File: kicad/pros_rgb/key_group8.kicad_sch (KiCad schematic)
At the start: 16 parts

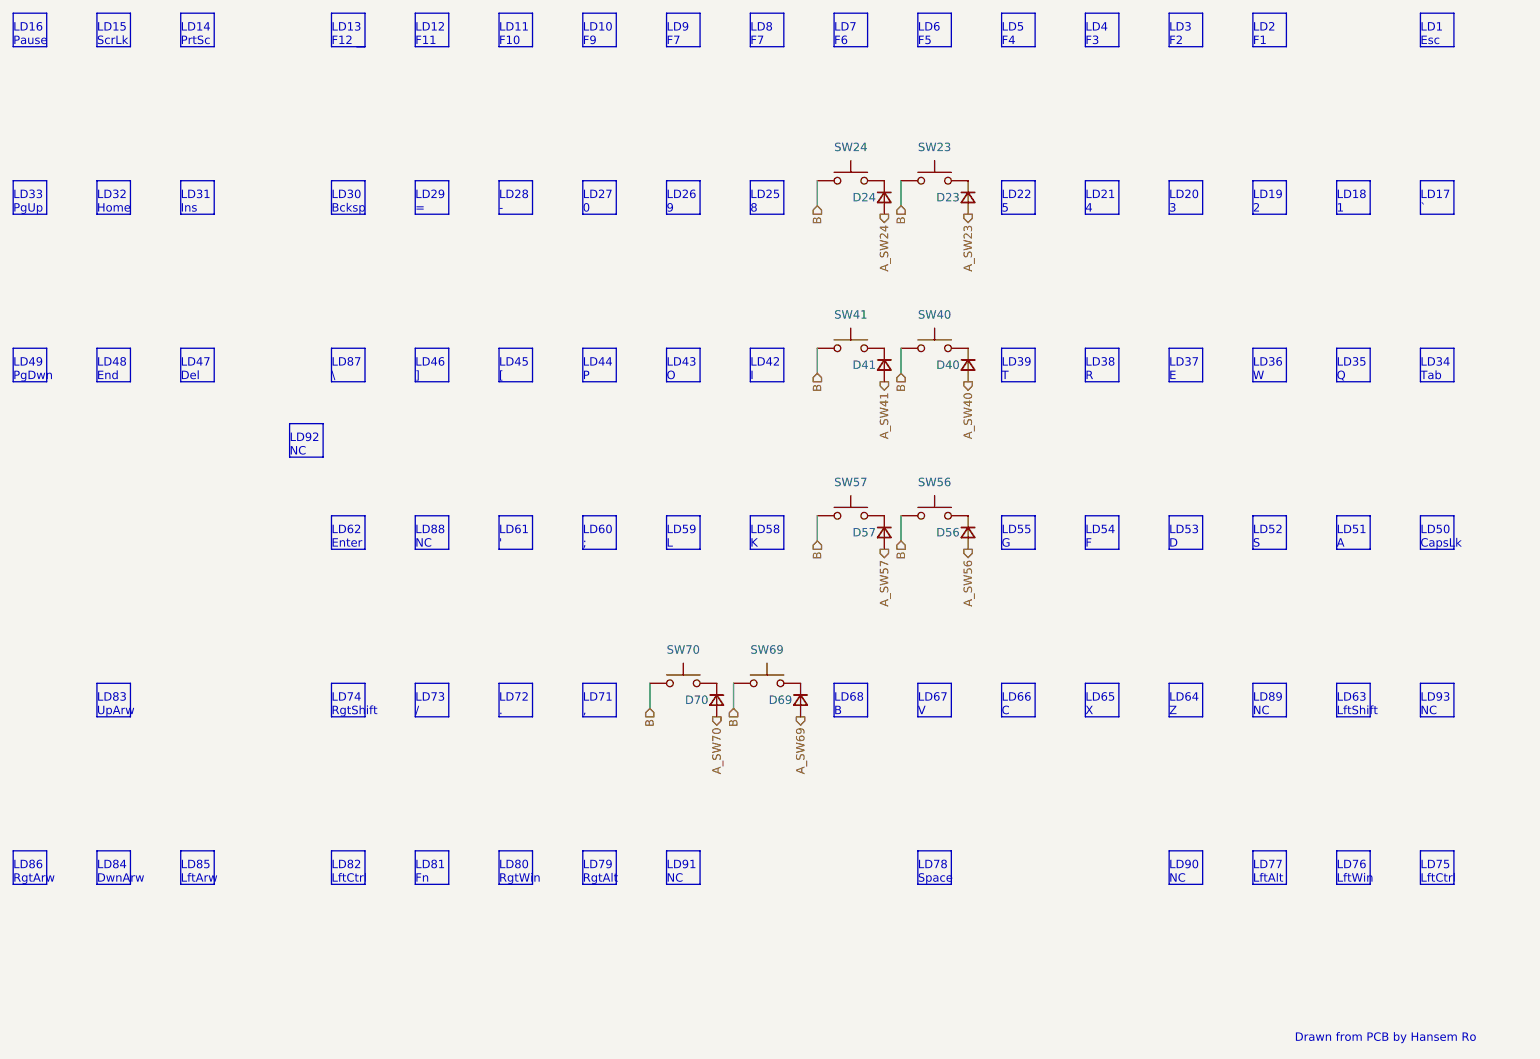
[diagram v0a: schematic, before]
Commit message: kicad/pros_rgb: update key groupings
These new groupings are based off ordering in firmware:
https://github.com/hansemro/pok3r_re_firmware/blob/4b68aa4baf7d28dc8dbf8eebcb1fdb59e7bcd629/disassemble/cmprosrgb/v122/cmprosrgb_v122.txt#L14599-L14629
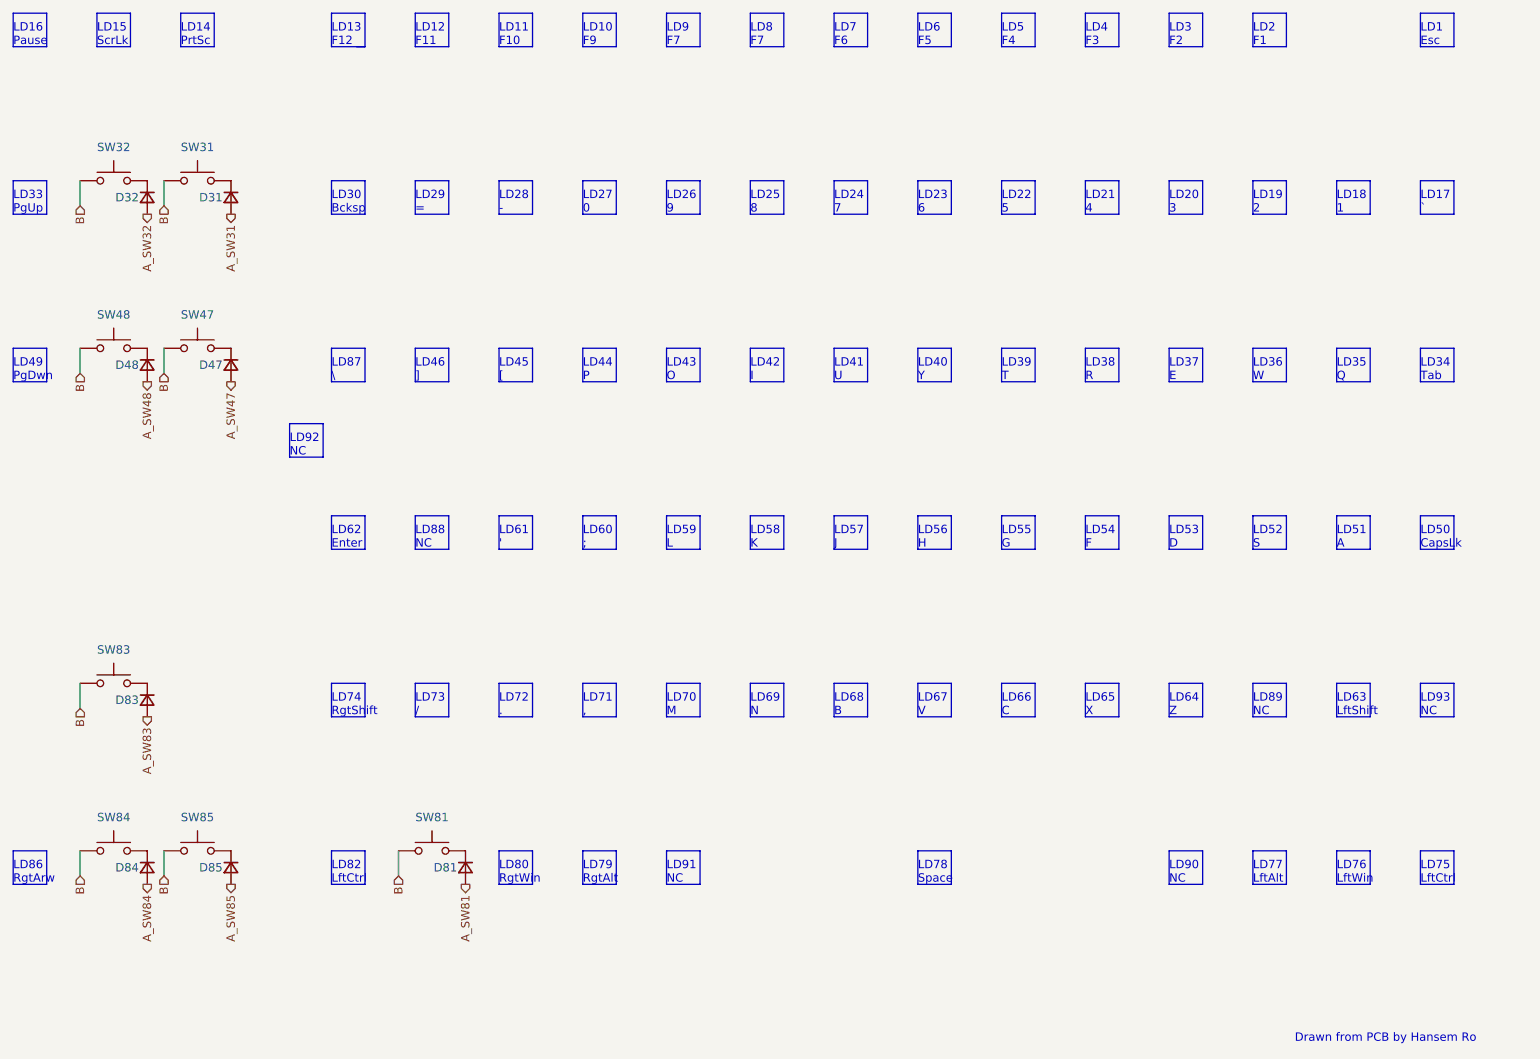
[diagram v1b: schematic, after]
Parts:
- removed D23, D24, D40, D41, D56, D57, D69, D70: ~, symbol Device:D_Small
- removed SW23, SW24, SW40, SW41, SW56, SW57, SW69, SW70: ~, symbol Switch:SW_Push
- added D31, D32, D47, D48, D81, D83, D84, D85: (no value), symbol Device:D_Small
- added SW31, SW32, SW47, SW48, SW81, SW83, SW84, SW85: (no value), symbol Switch:SW_Push
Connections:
- net B: now also SW31.1, SW32.1, SW47.1, SW48.1, SW81.1, SW83.1, SW84.1, SW85.1
- new net: D32.1 (K), SW32.2
- new net: D81.1 (K), SW81.2
- new net: D85.1 (K), SW85.2
- new net: D84.1 (K), SW84.2
- new net: D31.1 (K), SW31.2
- new net: D47.1 (K), SW47.2
- new net: D83.1 (K), SW83.2
- new net: D48.1 (K), SW48.2
- new net A_SW31: D31.2 (A)
- new net A_SW32: D32.2 (A)
- new net A_SW47: D47.2 (A)
- new net A_SW48: D48.2 (A)
- new net A_SW81: D81.2 (A)
- new net A_SW83: D83.2 (A)
- new net A_SW84: D84.2 (A)
- new net A_SW85: D85.2 (A)
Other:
- note added: "LD23 6"
- note added: "LD24 7"
- note added: "LD40 Y"
- note added: "LD41 U"
- note added: "LD56 H"
- note added: "LD57 J"
- note added: "LD69 N"
- note added: "LD70 M"
- note removed: "LD31 Ins"
- note removed: "LD32 Home"
- note removed: "LD47 Del"
- note removed: "LD48 End"
- note removed: "LD81 Fn"
- note removed: "LD83 UpArw"
- note removed: "LD84 DwnArw"
- note removed: "LD85 LftArw"

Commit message: kicad/pros_rgb: mark as Rev. B
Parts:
- D31, D32, D47, D48, D81, D83, D84, D85, SW31, SW32, SW47, SW48, SW81, SW83, SW84, SW85: value (none) -> ~
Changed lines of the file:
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@@
       (effects (font (size 1.27 1.27)) (justify right))
     )
-    (property "Value" "" (id 1) (at 81.28 53.3399 90)
+    (property "Value" "~" (id 1) (at 81.28 53.3399 90)
       (effects (font (size 1.27 1.27)) (justify left))
     )
@@
       (effects (font (size 1.27 1.27)) (justify right))
     )
-    (property "Value" "" (id 1) (at 129.54 154.9399 90)
+    (property "Value" "~" (id 1) (at 129.54 154.9399 90)
       (effects (font (size 1.27 1.27)) (justify left))
     )
@@
     (in_bom yes) (on_board yes)
     (property "Reference" "SW32" (id 0) (at 73.66 44.45 0))
-    (property "Value" "" (id 1) (at 73.66 44.45 0))
+    (property "Value" "~" (id 1) (at 73.66 44.45 0))
     (property "Footprint" "" (id 2) (at 73.66 44.45 0)
       (effects (font (size 1.27 1.27)) hide)
@@
     (in_bom yes) (on_board yes)
     (property "Reference" "SW85" (id 0) (at 86.36 146.05 0))
-    (property "Value" "" (id 1) (at 86.36 146.05 0))
+    (property "Value" "~" (id 1) (at 86.36 146.05 0))
     (property "Footprint" "" (id 2) (at 86.36 146.05 0)
       (effects (font (size 1.27 1.27)) hide)
@@
     (in_bom yes) (on_board yes)
     (property "Reference" "SW84" (id 0) (at 73.66 146.05 0))
-    (property "Value" "" (id 1) (at 73.66 146.05 0))
+    (property "Value" "~" (id 1) (at 73.66 146.05 0))
     (property "Footprint" "" (id 2) (at 73.66 146.05 0)
       (effects (font (size 1.27 1.27)) hide)
@@
       (effects (font (size 1.27 1.27)) (justify right))
     )
-    (property "Value" "" (id 1) (at 93.98 53.3399 90)
+    (property "Value" "~" (id 1) (at 93.98 53.3399 90)
       (effects (font (size 1.27 1.27)) (justify left))
     )
@@
     (in_bom yes) (on_board yes)
     (property "Reference" "SW47" (id 0) (at 86.36 69.85 0))
-    (property "Value" "" (id 1) (at 86.36 69.85 0))
+    (property "Value" "~" (id 1) (at 86.36 69.85 0))
     (property "Footprint" "" (id 2) (at 86.36 69.85 0)
       (effects (font (size 1.27 1.27)) hide)
@@
       (effects (font (size 1.27 1.27)) (justify right))
     )
-    (property "Value" "" (id 1) (at 81.28 129.5399 90)
+    (property "Value" "~" (id 1) (at 81.28 129.5399 90)
       (effects (font (size 1.27 1.27)) (justify left))
     )
@@
     (in_bom yes) (on_board yes)
     (property "Reference" "SW48" (id 0) (at 73.66 69.85 0))
-    (property "Value" "" (id 1) (at 73.66 69.85 0))
+    (property "Value" "~" (id 1) (at 73.66 69.85 0))
     (property "Footprint" "" (id 2) (at 73.66 69.85 0)
       (effects (font (size 1.27 1.27)) hide)
@@
     (in_bom yes) (on_board yes)
     (property "Reference" "SW31" (id 0) (at 86.36 44.45 0))
-    (property "Value" "" (id 1) (at 86.36 44.45 0))
+    (property "Value" "~" (id 1) (at 86.36 44.45 0))
     (property "Footprint" "" (id 2) (at 86.36 44.45 0)
       (effects (font (size 1.27 1.27)) hide)
@@
       (effects (font (size 1.27 1.27)) (justify right))
     )
-    (property "Value" "" (id 1) (at 81.28 154.9399 90)
+    (property "Value" "~" (id 1) (at 81.28 154.9399 90)
       (effects (font (size 1.27 1.27)) (justify left))
     )
@@
     (in_bom yes) (on_board yes)
     (property "Reference" "SW81" (id 0) (at 121.92 146.05 0))
-    (property "Value" "" (id 1) (at 121.92 146.05 0))
+    (property "Value" "~" (id 1) (at 121.92 146.05 0))
     (property "Footprint" "" (id 2) (at 121.92 146.05 0)
       (effects (font (size 1.27 1.27)) hide)
@@
       (effects (font (size 1.27 1.27)) (justify right))
     )
-    (property "Value" "" (id 1) (at 93.98 154.9399 90)
+    (property "Value" "~" (id 1) (at 93.98 154.9399 90)
       (effects (font (size 1.27 1.27)) (justify left))
     )
@@
     (in_bom yes) (on_board yes)
     (property "Reference" "SW83" (id 0) (at 73.66 120.65 0))
-    (property "Value" "" (id 1) (at 73.66 120.65 0))
+    (property "Value" "~" (id 1) (at 73.66 120.65 0))
     (property "Footprint" "" (id 2) (at 73.66 120.65 0)
       (effects (font (size 1.27 1.27)) hide)
@@
       (effects (font (size 1.27 1.27)) (justify right))
     )
-    (property "Value" "" (id 1) (at 81.28 78.7399 90)
+    (property "Value" "~" (id 1) (at 81.28 78.7399 90)
       (effects (font (size 1.27 1.27)) (justify left))
     )
@@
       (effects (font (size 1.27 1.27)) (justify right))
     )
-    (property "Value" "" (id 1) (at 93.98 78.7399 90)
-      (effects (font (size 1.27 1.27)) (justify left))
-    )
+    (property "Value" "~" (id 1) (at 93.98 78.7399 90)
+      (effects (font (size 1.27 1.27)) (justify left))
+    )

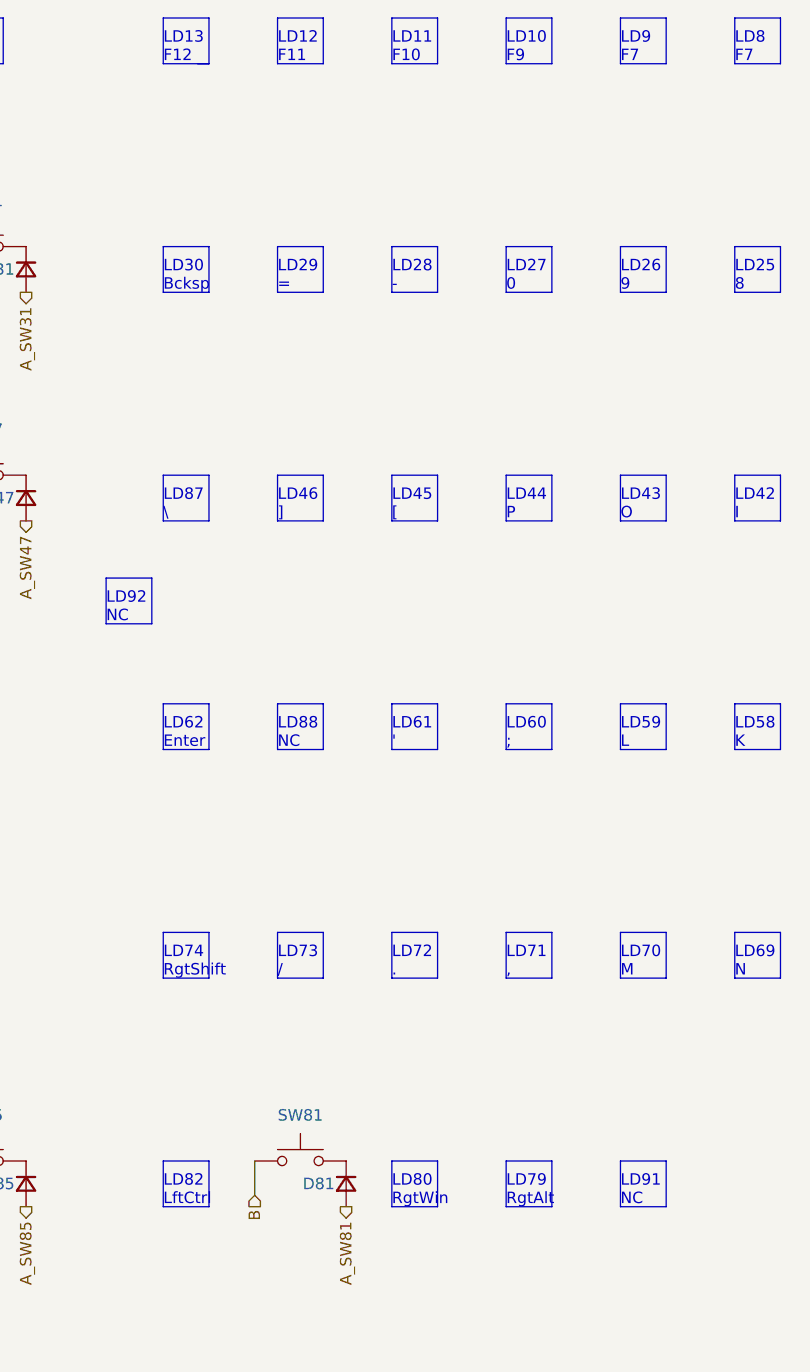
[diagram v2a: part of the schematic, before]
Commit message: kicad/pros_rgb: fix typos
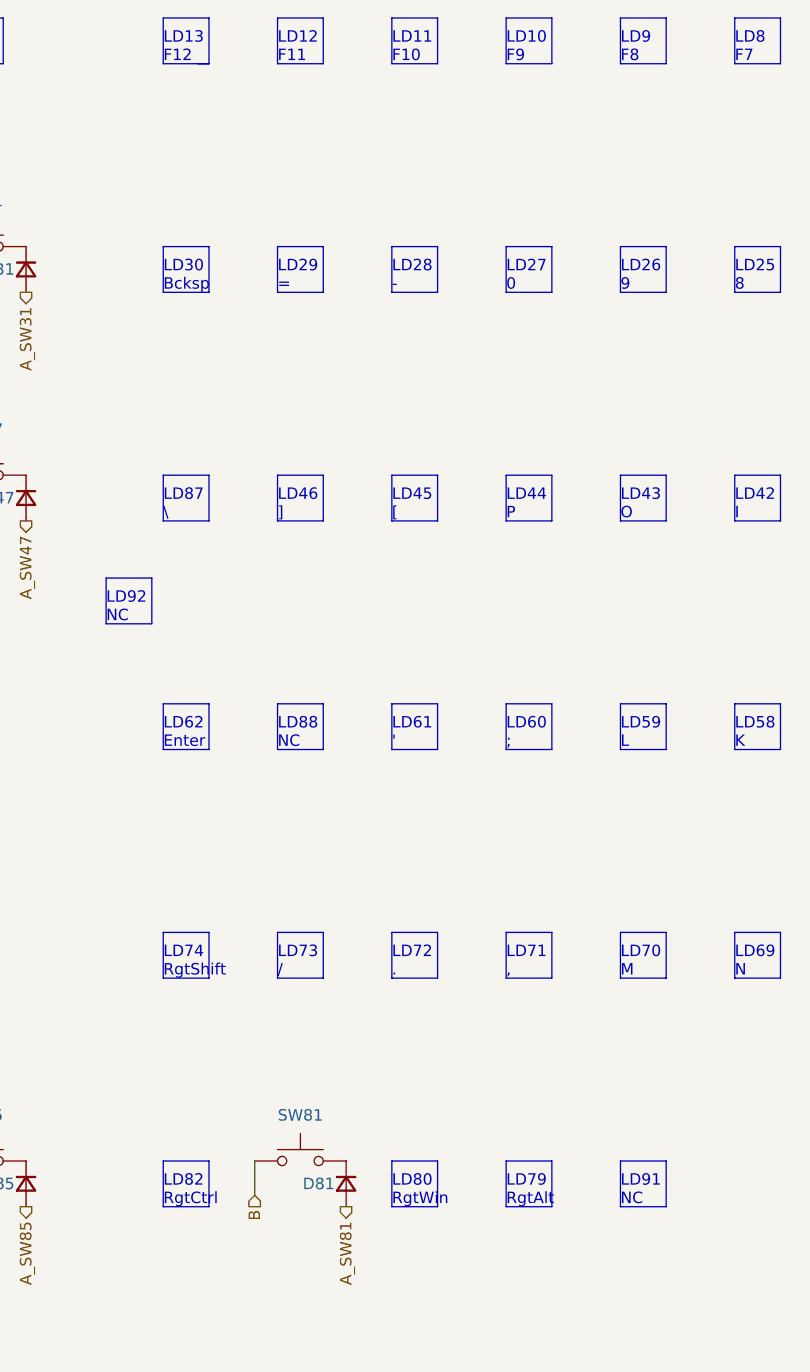
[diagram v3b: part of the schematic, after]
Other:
- note added: "LD82 RgtCtrl"
- note added: "LD9 F8"
- note removed: "LD82 LftCtrl"
- note removed: "LD9 F7"
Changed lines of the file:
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@@
     (effects (font (size 1.27 1.27)) (justify left bottom))
   )
-  (text "LD9\nF7" (at 157.48 29.21 0)
+  (text "LD9\nF8" (at 157.48 29.21 0)
     (effects (font (size 1.27 1.27)) (justify left bottom))
   )
@@
     (effects (font (size 1.27 1.27)) (justify left bottom))
   )
-  (text "LD82\nLftCtrl" (at 106.68 156.21 0)
+  (text "LD82\nRgtCtrl" (at 106.68 156.21 0)
     (effects (font (size 1.27 1.27)) (justify left bottom))
   )
